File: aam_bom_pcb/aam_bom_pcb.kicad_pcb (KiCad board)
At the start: 4 copper layers, 58 x 19.5 mm, 39 parts, among them J1 USB_C_Receptacle_USB2.0_16P, J2 Conn_ARM_SWD_TagConnect_TC203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, U1 BQ25120AYFPR, U3 STM32WB5MMG, U4 TLV320DAC3203IRGER

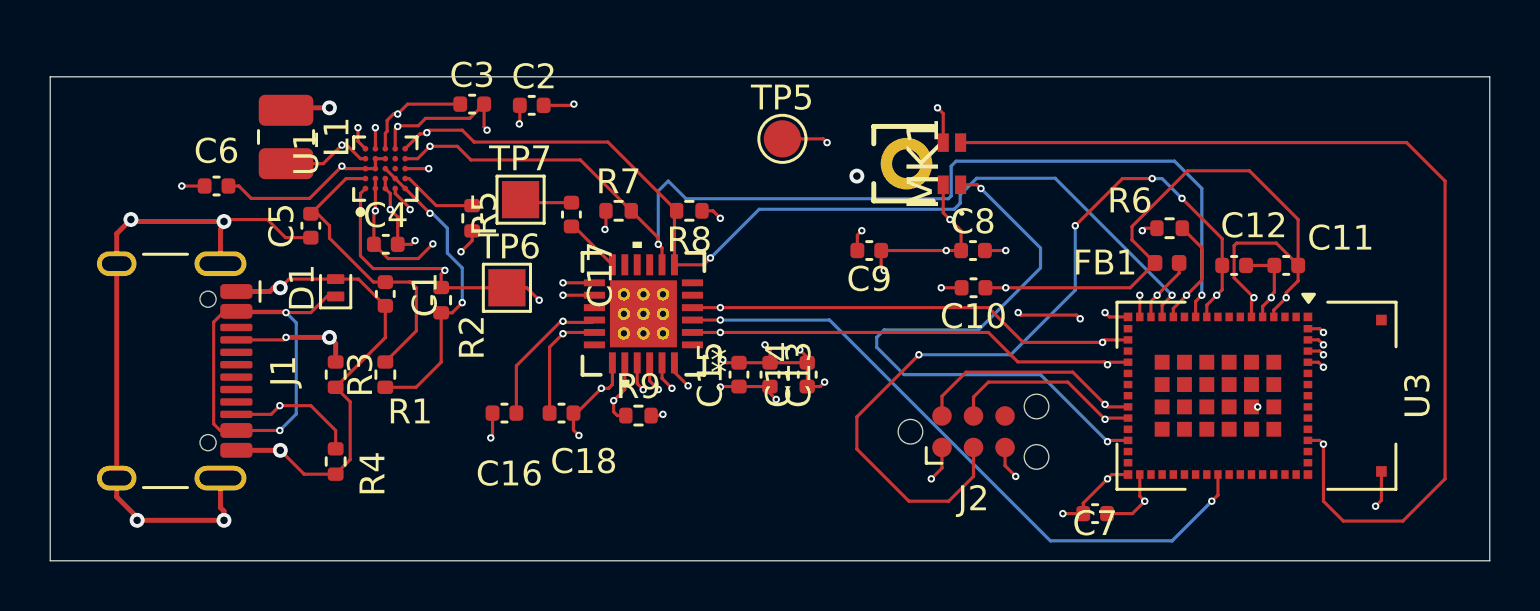
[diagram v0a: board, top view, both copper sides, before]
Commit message: Eliminar historial del editor y subir avances del QFN
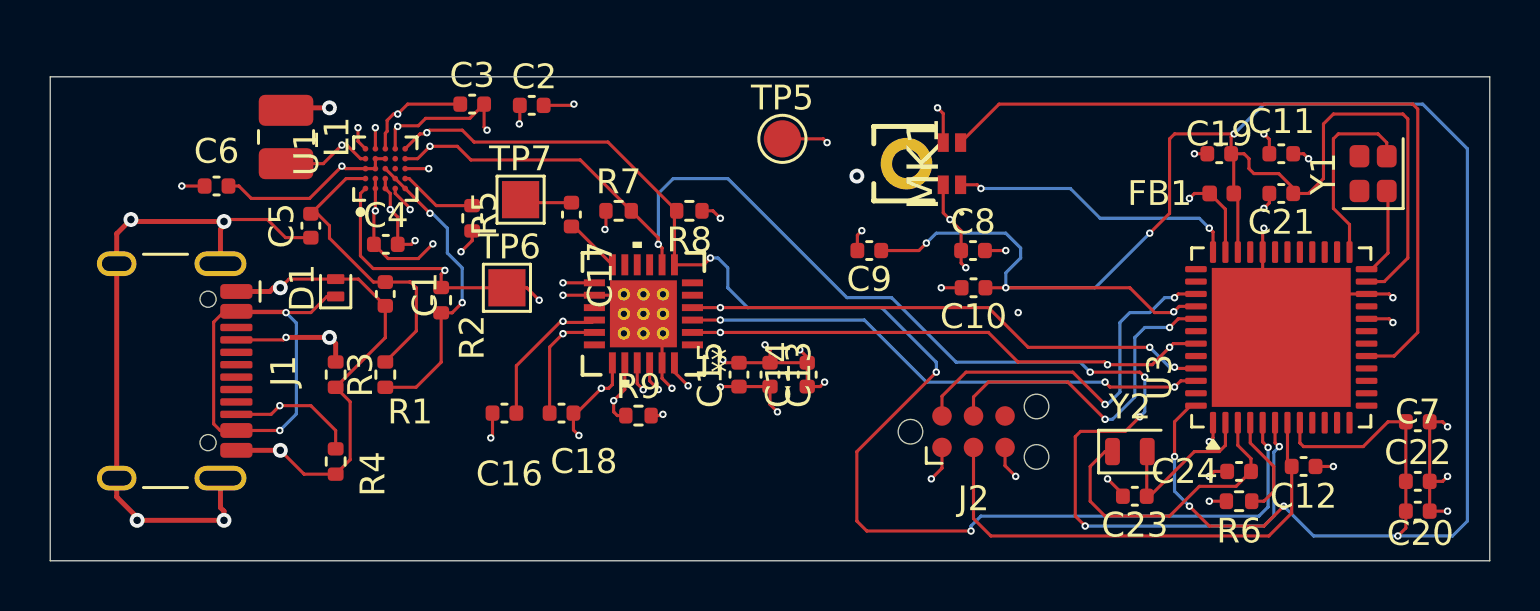
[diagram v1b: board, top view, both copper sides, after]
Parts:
- added C19: 100nF, Capacitor_SMD:C_0402_1005Metric, F.Cu at (208.6, 48.6)
- added C20: 100nF, Capacitor_SMD:C_0402_1005Metric, F.Cu at (216.6, 63.0)
- added C21: 100nF, Capacitor_SMD:C_0402_1005Metric, F.Cu at (211.1, 50.2)
- added C22: 100pF, Capacitor_SMD:C_0402_1005Metric, F.Cu at (216.6, 61.8)
- added C23: 15pF, Capacitor_SMD:C_0402_1005Metric, F.Cu at (205.2, 62.4)
- added C24: 10pF, Capacitor_SMD:C_0402_1005Metric, F.Cu at (209.4, 61.4)
- added Y1: Crystal, Crystal:Crystal_SMD_2016-4Pin_2.0x1.6mm, F.Cu at (214.8, 49.4)
- added Y2: Crystal, Crystal:Crystal_SMD_2012-2Pin_2.0x1.2mm, F.Cu at (205.0, 60.6)
- FB1: value FerriteBead -> 600R@100MHz
- R1: value 37k -> 37.4k
- R2: value 50k -> 49.9k
- U3: value STM32WB5MMG -> STM32WB55CGU6; footprint RF_Module:ST-SiP-LGA-86-11x7.3mm -> Package_DFN_QFN:QFN-48-1EP_7x7mm_P0.5mm_EP5.6x5.6mm
- moved C7 13.5 mm to (216.6, 59.4), turned to 0 degrees
- moved R6 11.4 mm to (209.4, 62.6)
- moved C12 8.57 mm to (212.0, 61.2)
- moved C11 4.50 mm to (211.1, 48.6), turned to 0 degrees
- moved FB1 3.56 mm to (208.7, 50.2)
- moved U3 2.55 mm to (211.1, 56.0), turned to 90 degrees
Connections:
- C10 pad 1: Net-(U3-VDDA) -> +1V8 MCU
- C11 pad 1: Net-(U3-VDDA) -> +1V8
- C7 pad 1: +1V8 -> +1V8 MCU
- C9 pad 1: +1V8 -> +1V8 MCU
- FB1 pad 1: Net-(U3-VDDA) -> +1V8
- FB1 pad 2: +1V8 -> +1V8 MCU
- R6 pad 1: Net-(U3-PH3-BOOT0) -> Net-(U3-PH3)
- U3 pad 1: unconnected-(U3-PA2-Pad1) -> +1V8
- U3 pad 10: /SWD_NRST -> unconnected-(U3-PA1-Pad10)
- U3 pad 11: I2C_SDA -> unconnected-(U3-PA2-Pad11)
- U3 pad 13: Net-(U3-PH3-BOOT0) -> unconnected-(U3-PA4-Pad13)
- U3 pad 14: I2C_SCL -> unconnected-(U3-PA5-Pad14)
- U3 pad 15: +1V8 -> unconnected-(U3-PA6-Pad15)
- U3 pad 16: GND -> unconnected-(U3-PA7-Pad16)
- U3 pad 17: +1V8 -> PDM_CLK
- U3 pad 19: /I2S_DIN -> unconnected-(U3-PB2-Pad19)
- U3 pad 2: unconnected-(U3-PA1-Pad2) -> Net-(U3-PC14)
- U3 pad 20: unconnected-(U3-PB4-Pad20) -> +1V8
- U3 pad 21: /I2S_BCLK -> unconnected-(U3-RF1-Pad21)
- U3 pad 22: unconnected-(U3-PC10-Pad22) -> GND
- U3 pad 23: unconnected-(U3-PC11-Pad23) -> +1V8 MCU
- U3 pad 24: unconnected-(U3-PC12-Pad24) -> Net-(U3-OSC_OUT)
- U3 pad 25: /SWDIO -> Net-(U3-OSC_IN)
- U3 pad 26: /SWCLK -> unconnected-(U3-AT0-Pad26)
- U3 pad 28: PDM_DATA -> unconnected-(U3-PB0-Pad28)
- U3 pad 3: unconnected-(U3-PA0-Pad3) -> Net-(U3-PC15)
- U3 pad 31: GND -> unconnected-(U3-VFBSMPS-Pad31)
- U3 pad 32: +1V8 -> GND
- U3 pad 34: unconnected-(U3-PD1-Pad34) -> +1V8 MCU
- U3 pad 35: unconnected-(U3-PB13-Pad35) -> +1V8
- U3 pad 36: unconnected-(U3-PC6-Pad36) -> PDM_DATA
- U3 pad 39: /I2S_WCLK -> /SWDIO
- U3 pad 4: Net-(U3-VDDA) -> Net-(U3-PH3)
- U3 pad 40: unconnected-(U3-PC13-Pad40) -> +1V8 MCU
- U3 pad 41: unconnected-(U3-PB12-Pad41) -> /SWCLK
- U3 pad 43: unconnected-(U3-PB1-Pad43) -> /I2S_BCLK
- U3 pad 45: unconnected-(U3-PC5-Pad45) -> /I2S_DIN
- U3 pad 46: unconnected-(U3-PB11-Pad46) -> /I2S_WCLK
- U3 pad 48: unconnected-(U3-PB2-Pad48) -> +1V8 MCU
- U3 pad 49: unconnected-(U3-PC4-Pad49) -> GND
- U3 pad 5: GND -> I2C_SCL
- U3 pad 6: Net-(U3-VDDA) -> I2C_SDA
- U3 pad 7: unconnected-(U3-PC3-Pad7) -> /SWD_NRST
- U3 pad 8: unconnected-(U3-PC2-Pad8) -> +1V8 MCU
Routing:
- net +1V8 MCU: track 0.00 -> 107.3 mm, vias 0 -> 9
- net Net-(U3-VDDA): track 28.1 -> 0.00 mm, vias 3 -> 0
- net I2C_SCL: track 39.6 -> 56.2 mm, vias 3 -> 5
- net I2C_SDA: track 44.7 -> 58.4 mm, vias 3 -> 7
- net PDM_DATA: track 25.0 -> 11.8 mm
- net GND: track 239.0 -> 252.0 mm, vias 41 -> 42
- net /SWD_NRST: track 33.1 -> 20.1 mm, vias 5 -> 0
- net Net-(U3-PC15): track 0.00 -> 12.2 mm
- net PDM_CLK: track 41.1 -> 30.6 mm, vias 1 -> 0
- net +1V8: track 135.5 -> 144.0 mm, vias 21 -> 20
- net Net-(U3-OSC_IN): track 0.00 -> 7.76 mm
- net Net-(U3-PC14): track 0.00 -> 6.74 mm
- net /SWDIO: track 9.27 -> 15.5 mm, vias 1 -> 2
- net /SWCLK: track 7.88 -> 13.8 mm, vias 1 -> 2
- net /I2S_WCLK: track 26.5 -> 21.5 mm, vias 2 -> 3
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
